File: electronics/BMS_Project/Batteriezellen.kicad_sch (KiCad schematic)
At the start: 4 parts

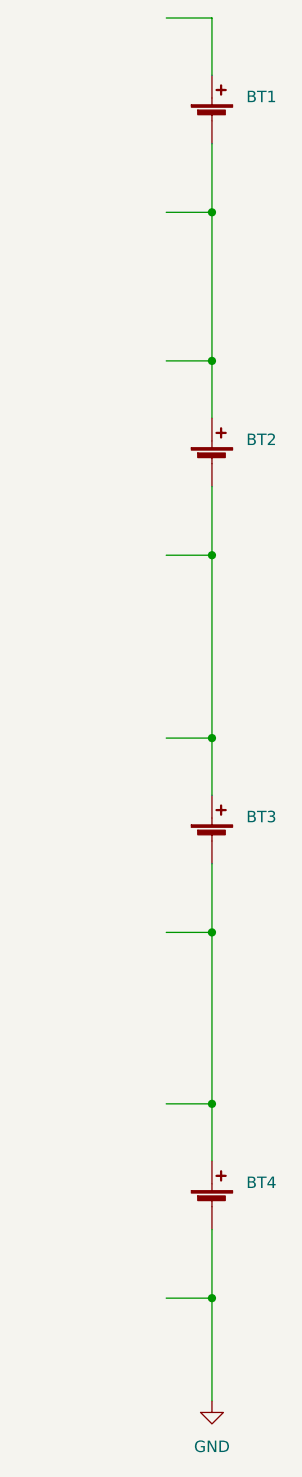
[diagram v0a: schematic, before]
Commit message: Started working on schematic segmentation and added first labels
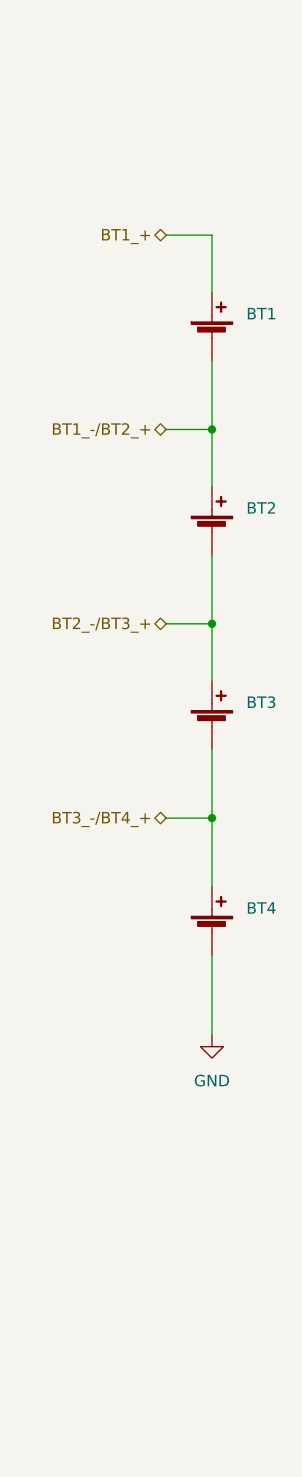
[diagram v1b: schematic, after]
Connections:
- net BT3_-/BT4_+: now reaches BT3.2 (-), BT4.1 (+)
- net BT1_+: now reaches BT1.1 (+)
- net BT1_-/BT2_+: now reaches BT1.2 (-), BT2.1 (+)
- net BT2_-/BT3_+: now reaches BT2.2 (-), BT3.1 (+)
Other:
- moved on the sheet: BT1, BT2, BT3, BT4
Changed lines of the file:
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@@
     (comment 2 "Edited: ")
   )
-  (junction (at 105.41 167.64) (diameter 0) (color 0 0 0 0)
+  (junction (at 105.41 71.12) (diameter 0) (color 0 0 0 0)
   )
-  (junction (at 105.41 85.09) (diameter 0) (color 0 0 0 0)
+  (junction (at 105.41 114.3) (diameter 0) (color 0 0 0 0)
   )
-  (junction (at 105.41 127) (diameter 0) (color 0 0 0 0)
+  (junction (at 105.41 92.71) (diameter 0) (color 0 0 0 0)
   )
-  (junction (at 105.41 46.99) (diameter 0) (color 0 0 0 0)
-  )
-  (junction (at 105.41 63.5) (diameter 0) (color 0 0 0 0)
-  )
-  (junction (at 105.41 105.41) (diameter 0) (color 0 0 0 0)
-  )
-  (junction (at 105.41 146.05) (diameter 0) (color 0 0 0 0)
-  )
-  (wire (pts (xy 105.41 46.99) (xy 105.41 63.5))
+  (wire (pts (xy 105.41 63.5) (xy 105.41 71.12))
     (stroke (width 0) (type default))
   )
-  (wire (pts (xy 105.41 39.37) (xy 105.41 46.99))
+  (wire (pts (xy 105.41 114.3) (xy 100.33 114.3))
     (stroke (width 0) (type default))
   )
-  (wire (pts (xy 100.33 146.05) (xy 105.41 146.05))
+  (wire (pts (xy 105.41 71.12) (xy 100.33 71.12))
     (stroke (width 0) (type default))
   )
-  (wire (pts (xy 105.41 127) (xy 100.33 127))
+  (wire (pts (xy 105.41 71.12) (xy 105.41 77.47))
     (stroke (width 0) (type default))
   )
-  (wire (pts (xy 105.41 160.02) (xy 105.41 167.64))
+  (wire (pts (xy 105.41 49.53) (xy 105.41 55.88))
     (stroke (width 0) (type default))
   )
-  (wire (pts (xy 100.33 63.5) (xy 105.41 63.5))
+  (wire (pts (xy 100.33 49.53) (xy 105.41 49.53))
     (stroke (width 0) (type default))
   )
-  (wire (pts (xy 105.41 46.99) (xy 100.33 46.99))
+  (wire (pts (xy 105.41 92.71) (xy 105.41 99.06))
     (stroke (width 0) (type default))
   )
-  (wire (pts (xy 105.41 63.5) (xy 105.41 69.85))
+  (wire (pts (xy 105.41 85.09) (xy 105.41 92.71))
     (stroke (width 0) (type default))
   )
-  (wire (pts (xy 105.41 25.4) (xy 105.41 31.75))
+  (wire (pts (xy 105.41 92.71) (xy 100.33 92.71))
     (stroke (width 0) (type default))
   )
-  (wire (pts (xy 100.33 25.4) (xy 105.41 25.4))
+  (wire (pts (xy 105.41 106.68) (xy 105.41 114.3))
     (stroke (width 0) (type default))
   )
-  (wire (pts (xy 105.41 85.09) (xy 105.41 105.41))
+  (wire (pts (xy 105.41 114.3) (xy 105.41 121.92))
     (stroke (width 0) (type default))
   )
-  (wire (pts (xy 105.41 146.05) (xy 105.41 152.4))
+  (wire (pts (xy 105.41 129.54) (xy 105.41 138.43))
     (stroke (width 0) (type default))
   )
-  (wire (pts (xy 105.41 105.41) (xy 105.41 111.76))
-    (stroke (width 0) (type default))
+  (hierarchical_label "BT3_-{slash}BT4_+" (shape bidirectional) (at 100.33 114.3 180) (fields_autoplaced)
+    (effects (font (size 1.27 1.27)) (justify right))
   )
-  (wire (pts (xy 100.33 105.41) (xy 105.41 105.41))
-    (stroke (width 0) (type default))
+  (hierarchical_label "BT1_+" (shape bidirectional) (at 100.33 49.53 180) (fields_autoplaced)
+    (effects (font (size 1.27 1.27)) (justify right))
   )
-  (wire (pts (xy 105.41 77.47) (xy 105.41 85.09))
-    (stroke (width 0) (type default))
+  (hierarchical_label "BT2_-{slash}BT3_+" (shape bidirectional) (at 100.33 92.71 180) (fields_autoplaced)
+    (effects (font (size 1.27 1.27)) (justify right))
   )
-  (wire (pts (xy 105.41 85.09) (xy 100.33 85.09))
-    (stroke (width 0) (type default))
+  (hierarchical_label "BT1_-{slash}BT2_+" (shape bidirectional) (at 100.33 71.12 180) (fields_autoplaced)
+    (effects (font (size 1.27 1.27)) (justify right))
   )
-  (wire (pts (xy 105.41 119.38) (xy 105.41 127))
-    (stroke (width 0) (type default))
-  )
-  (wire (pts (xy 105.41 127) (xy 105.41 146.05))
-    (stroke (width 0) (type default))
-  )
-  (wire (pts (xy 105.41 167.64) (xy 100.33 167.64))
-    (stroke (width 0) (type default))
-  )
-  (wire (pts (xy 105.41 167.64) (xy 105.41 179.07))
-    (stroke (width 0) (type default))
-  )
-  (symbol (lib_id "Device:Battery_Cell") (at 105.41 157.48 0) (unit 1)
+  (symbol (lib_id "Device:Battery_Cell") (at 105.41 127 0) (unit 1)
     (in_bom yes) (on_board yes) (dnp no) (fields_autoplaced)
-    (property "Reference" "BT4" (at 109.22 154.813 0)
+    (property "Reference" "BT4" (at 109.22 124.333 0)
       (effects (font (size 1.27 1.27)) (justify left))
     )
-    (property "Value" "Battery_Cell" (at 109.22 157.353 0)
+    (property "Value" "Battery_Cell" (at 109.22 126.873 0)
       (effects (font (size 1.27 1.27)) (justify left) hide)
     )
-    (property "Footprint" "" (at 105.41 155.956 90)
+    (property "Footprint" "" (at 105.41 125.476 90)
       (effects (font (size 1.27 1.27)) hide)
     )
-    (property "Datasheet" "~" (at 105.41 155.956 90)
+    (property "Datasheet" "~" (at 105.41 125.476 90)
       (effects (font (size 1.27 1.27)) hide)
     )
@@
     )
   )
-  (symbol (lib_id "Device:Battery_Cell") (at 105.41 36.83 0) (unit 1)
+  (symbol (lib_id "Device:Battery_Cell") (at 105.41 60.96 0) (unit 1)
     (in_bom yes) (on_board yes) (dnp no) (fields_autoplaced)
-    (property "Reference" "BT1" (at 109.22 34.163 0)
+    (property "Reference" "BT1" (at 109.22 58.293 0)
       (effects (font (size 1.27 1.27)) (justify left))
     )
-    (property "Value" "Battery_Cell" (at 109.22 36.703 0)
+    (property "Value" "Battery_Cell" (at 109.22 60.833 0)
       (effects (font (size 1.27 1.27)) (justify left) hide)
     )
-    (property "Footprint" "" (at 105.41 35.306 90)
+    (property "Footprint" "" (at 105.41 59.436 90)
       (effects (font (size 1.27 1.27)) hide)
     )
-    (property "Datasheet" "~" (at 105.41 35.306 90)
+    (property "Datasheet" "~" (at 105.41 59.436 90)
       (effects (font (size 1.27 1.27)) hide)
     )
@@
     )
   )
-  (symbol (lib_id "Device:Battery_Cell") (at 105.41 116.84 0) (unit 1)
+  (symbol (lib_id "Device:Battery_Cell") (at 105.41 104.14 0) (unit 1)
     (in_bom yes) (on_board yes) (dnp no) (fields_autoplaced)
-    (property "Reference" "BT3" (at 109.22 114.173 0)
+    (property "Reference" "BT3" (at 109.22 101.473 0)
       (effects (font (size 1.27 1.27)) (justify left))
     )
-    (property "Value" "Battery_Cell" (at 109.22 116.713 0)
+    (property "Value" "Battery_Cell" (at 109.22 104.013 0)
       (effects (font (size 1.27 1.27)) (justify left) hide)
     )
-    (property "Footprint" "" (at 105.41 115.316 90)
+    (property "Footprint" "" (at 105.41 102.616 90)
       (effects (font (size 1.27 1.27)) hide)
     )
-    (property "Datasheet" "~" (at 105.41 115.316 90)
+    (property "Datasheet" "~" (at 105.41 102.616 90)
       (effects (font (size 1.27 1.27)) hide)
     )
@@
     )
   )
-  (symbol (lib_id "Device:Battery_Cell") (at 105.41 74.93 0) (unit 1)
+  (symbol (lib_id "Device:Battery_Cell") (at 105.41 82.55 0) (unit 1)
     (in_bom yes) (on_board yes) (dnp no) (fields_autoplaced)
-    (property "Reference" "BT2" (at 109.22 72.263 0)
+    (property "Reference" "BT2" (at 109.22 79.883 0)
       (effects (font (size 1.27 1.27)) (justify left))
     )
-    (property "Value" "Battery_Cell" (at 109.22 74.803 0)
+    (property "Value" "Battery_Cell" (at 109.22 82.423 0)
       (effects (font (size 1.27 1.27)) (justify left) hide)
     )
-    (property "Footprint" "" (at 105.41 73.406 90)
+    (property "Footprint" "" (at 105.41 81.026 90)
       (effects (font (size 1.27 1.27)) hide)
     )
-    (property "Datasheet" "~" (at 105.41 73.406 90)
+    (property "Datasheet" "~" (at 105.41 81.026 90)
       (effects (font (size 1.27 1.27)) hide)
     )
@@
     )
   )
-  (symbol (lib_id "power:GND") (at 105.41 179.07 0) (unit 1)
+  (symbol (lib_id "power:GND") (at 105.41 138.43 0) (unit 1)
     (in_bom yes) (on_board yes) (dnp no) (fields_autoplaced)
-    (property "Reference" "#PWR09" (at 105.41 185.42 0)
+    (property "Reference" "#PWR09" (at 105.41 144.78 0)
       (effects (font (size 1.27 1.27)) hide)
     )
-    (property "Value" "GND" (at 105.41 184.15 0)
+    (property "Value" "GND" (at 105.41 143.51 0)
       (effects (font (size 1.27 1.27)))
     )
-    (property "Footprint" "" (at 105.41 179.07 0)
+    (property "Footprint" "" (at 105.41 138.43 0)
       (effects (font (size 1.27 1.27)) hide)
     )
-    (property "Datasheet" "" (at 105.41 179.07 0)
+    (property "Datasheet" "" (at 105.41 138.43 0)
       (effects (font (size 1.27 1.27)) hide)
     )
